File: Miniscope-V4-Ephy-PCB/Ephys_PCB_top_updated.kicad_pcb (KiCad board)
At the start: 6 copper layers, 13 x 10 mm, 41 parts, among them J1 34 Circuit Slimslack Connector, J10 Conn_01x01, J11 Conn_01x01, J12 Conn_01x01, J13 Conn_01x01, J4 Conn_01x01, J5 Conn_01x01, J8 Conn_01x01, U1 ATSAME70N21A-CN, U2 RHD2132_QFN-RHD2132, U3 TLV7103318DSER, U4 TXB0304RUT, Y1 ABM8G-12.000MHZ-4Y-T3

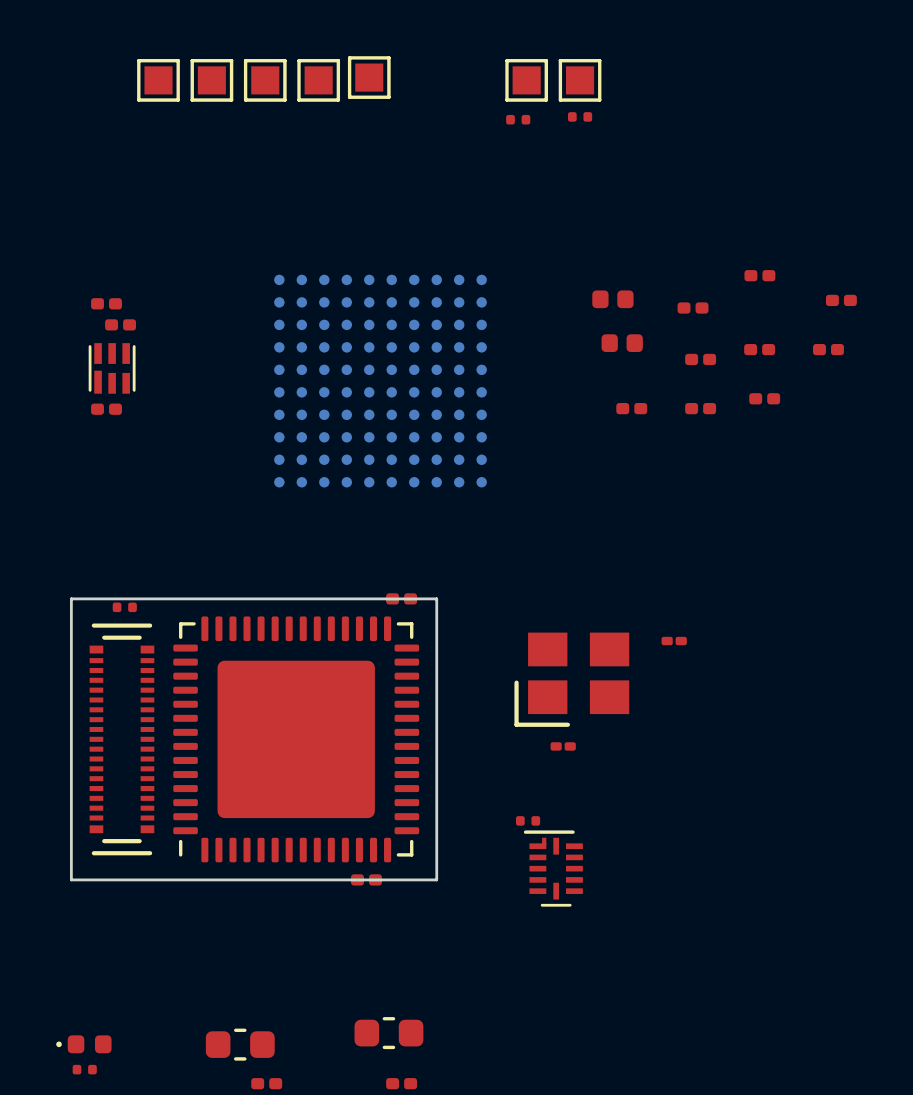
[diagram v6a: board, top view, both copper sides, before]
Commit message: Move around PCB layout a bit and initial route of electrode traces.
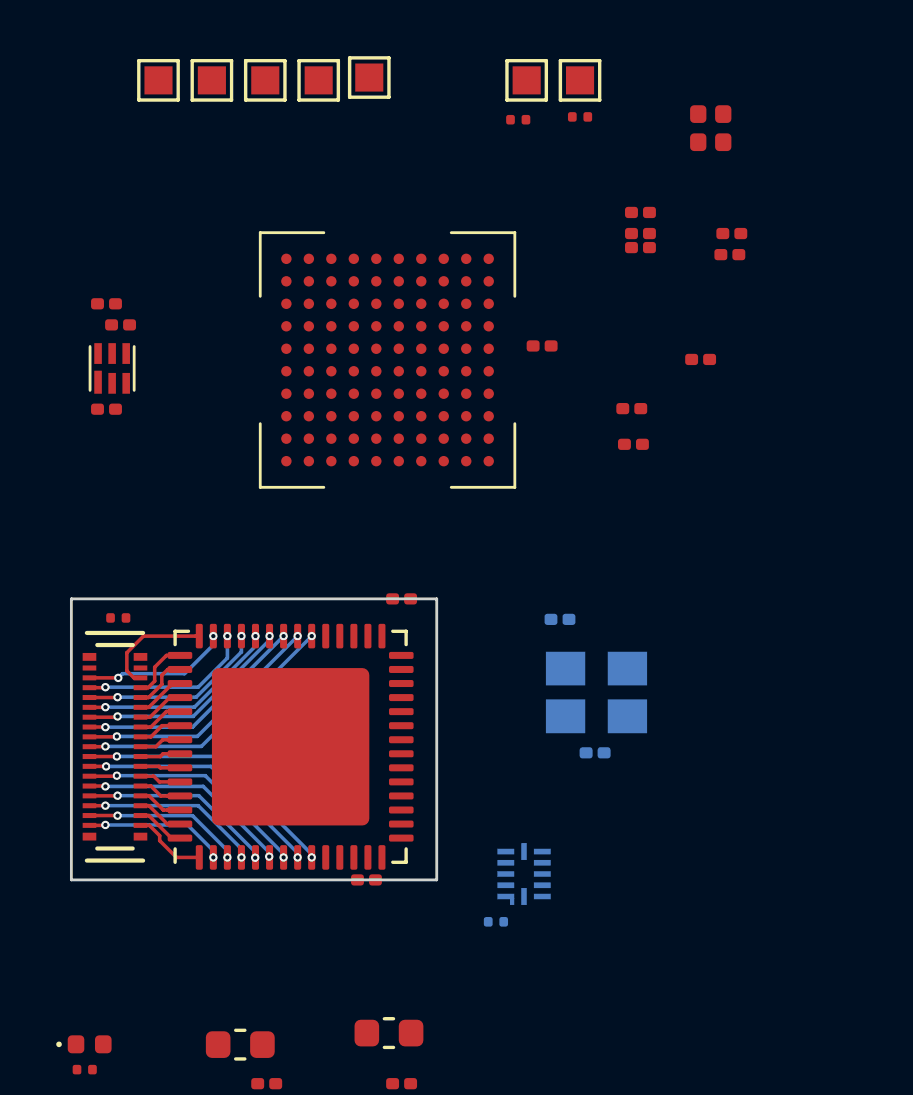
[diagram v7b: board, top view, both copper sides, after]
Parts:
- C17, C18: value GRM1555C1H120JA01D -> GRM033R60J105MEA2D; footprint Capacitor_SMD:C_01005_0402Metric -> Capacitor_SMD:C_0201_0603Metric; moved to B.Cu
- R2, U4, Y1: moved to B.Cu
- U1: moved to F.Cu
- moved C1 8.74 mm to (112.8, 72.8)
- moved C4 7.97 mm to (110.2, 76.2)
- moved C5 7.86 mm to (110.2, 77.0)
- moved C12 7.50 mm to (110.0, 84.5)
- moved C3 6.58 mm to (112.8, 73.8)
- moved C2 6.06 mm to (106.8, 81.0)
- moved C18 4.87 mm to (108.6, 95.5), turned to 180 degrees
- moved C8 4.57 mm to (113.5, 77.0)
- moved C17 4.52 mm to (107.4, 90.7)
- moved R2 3.77 mm to (105.1, 101.5)
- moved C9 3.54 mm to (113.4, 77.8)
- moved C6 2.85 mm to (110.2, 77.5)
- moved U4 1.16 mm to (106.1, 99.8)
- moved Y1 0.93 mm to (108.7, 93.3)
- moved U1 0.79 mm to (101.2, 81.5)
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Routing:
- net /IN31: track 0.00 -> 9.54 mm, vias 0 -> 2
- net /IN0: track 0.00 -> 9.46 mm, vias 0 -> 2
- net /IN30: track 0.00 -> 8.89 mm, vias 0 -> 2
- net /IN1: track 0.00 -> 8.84 mm, vias 0 -> 2
- net /IN29: track 0.00 -> 8.25 mm, vias 0 -> 2
- net /IN2: track 0.00 -> 8.19 mm, vias 0 -> 2
- net /IN28: track 0.00 -> 7.69 mm, vias 0 -> 2
- net /IN3: track 0.00 -> 7.52 mm, vias 0 -> 2
- net /IN27: track 0.00 -> 7.16 mm, vias 0 -> 2
- net /IN4: track 0.00 -> 6.93 mm, vias 0 -> 2
- net /IN26: track 0.00 -> 6.64 mm, vias 0 -> 2
- net /IN5: track 0.00 -> 6.35 mm, vias 0 -> 2
- net /IN25: track 0.00 -> 6.12 mm, vias 0 -> 2
- net /IN6: track 0.00 -> 5.67 mm, vias 0 -> 2
- net /IN24: track 0.00 -> 5.21 mm, vias 0 -> 2
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
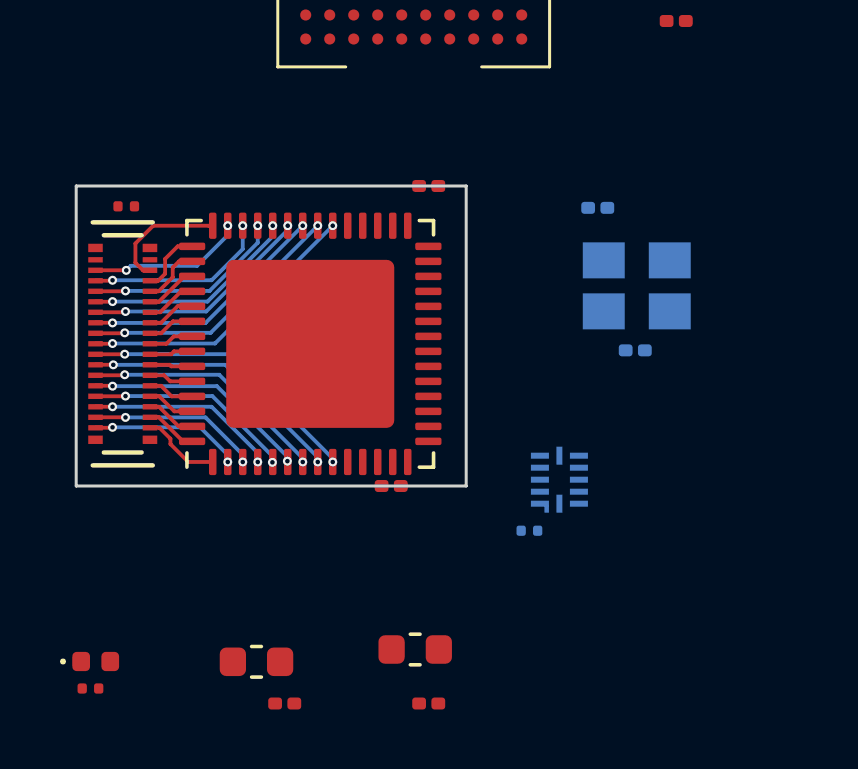
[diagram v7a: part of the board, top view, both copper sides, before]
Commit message: Move to new KiCad project for multi-board Ephys layout
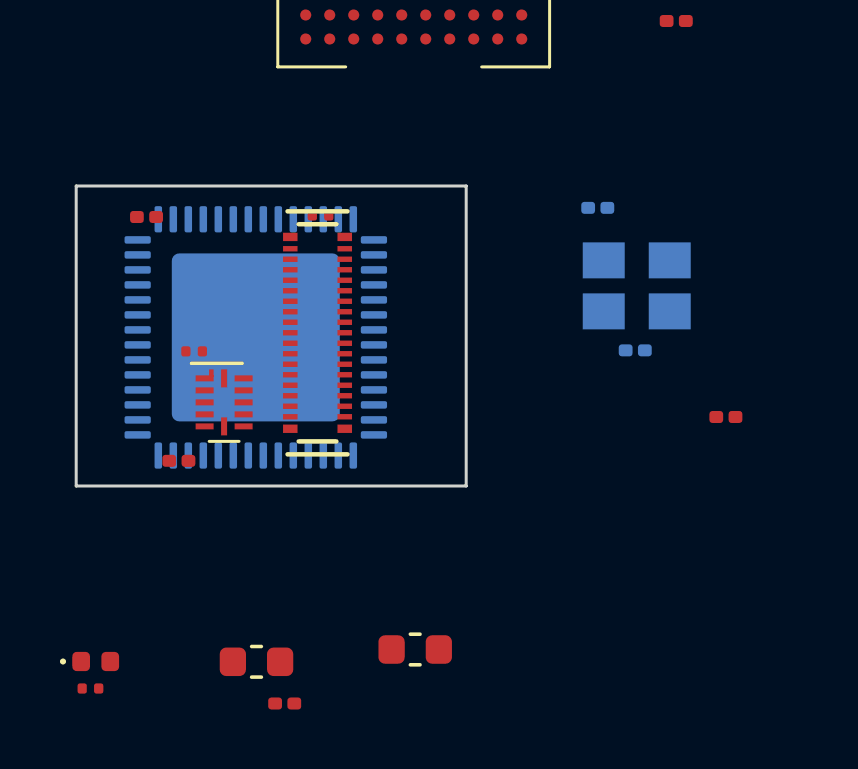
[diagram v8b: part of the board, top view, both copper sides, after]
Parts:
- R2, U4: moved to F.Cu
- U2: moved to B.Cu
- moved C16 13.8 mm to (111.7, 97.7)
- moved R2 12.7 mm to (93.9, 95.5)
- moved U4 11.5 mm to (94.9, 97.2)
- moved C14 9.46 mm to (92.3, 91.0), turned to 0 degrees
- moved C15 7.13 mm to (93.4, 99.2), turned to 0 degrees
- moved J1 6.50 mm to (98.0, 94.9)
- moved R1 6.48 mm to (98.1, 91.0)
- moved U2 1.83 mm to (96.0, 95.0)
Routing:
- net /IN31: track 9.54 -> 0.00 mm, vias 2 -> 0
- net /IN0: track 9.46 -> 0.00 mm, vias 2 -> 0
- net /IN30: track 8.89 -> 0.00 mm, vias 2 -> 0
- net /IN1: track 8.84 -> 0.00 mm, vias 2 -> 0
- net /IN29: track 8.25 -> 0.00 mm, vias 2 -> 0
- net /IN2: track 8.19 -> 0.00 mm, vias 2 -> 0
- net /IN28: track 7.69 -> 0.00 mm, vias 2 -> 0
- net /IN3: track 7.52 -> 0.00 mm, vias 2 -> 0
- net /IN27: track 7.16 -> 0.00 mm, vias 2 -> 0
- net /IN4: track 6.93 -> 0.00 mm, vias 2 -> 0
- net /IN26: track 6.64 -> 0.00 mm, vias 2 -> 0
- net /IN5: track 6.35 -> 0.00 mm, vias 2 -> 0
- net /IN25: track 6.12 -> 0.00 mm, vias 2 -> 0
- net /IN6: track 5.67 -> 0.00 mm, vias 2 -> 0
- net /IN24: track 5.21 -> 0.00 mm, vias 2 -> 0
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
